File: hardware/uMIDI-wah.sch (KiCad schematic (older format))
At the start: 12 parts, among them U1 Opamp_Dual_Generic

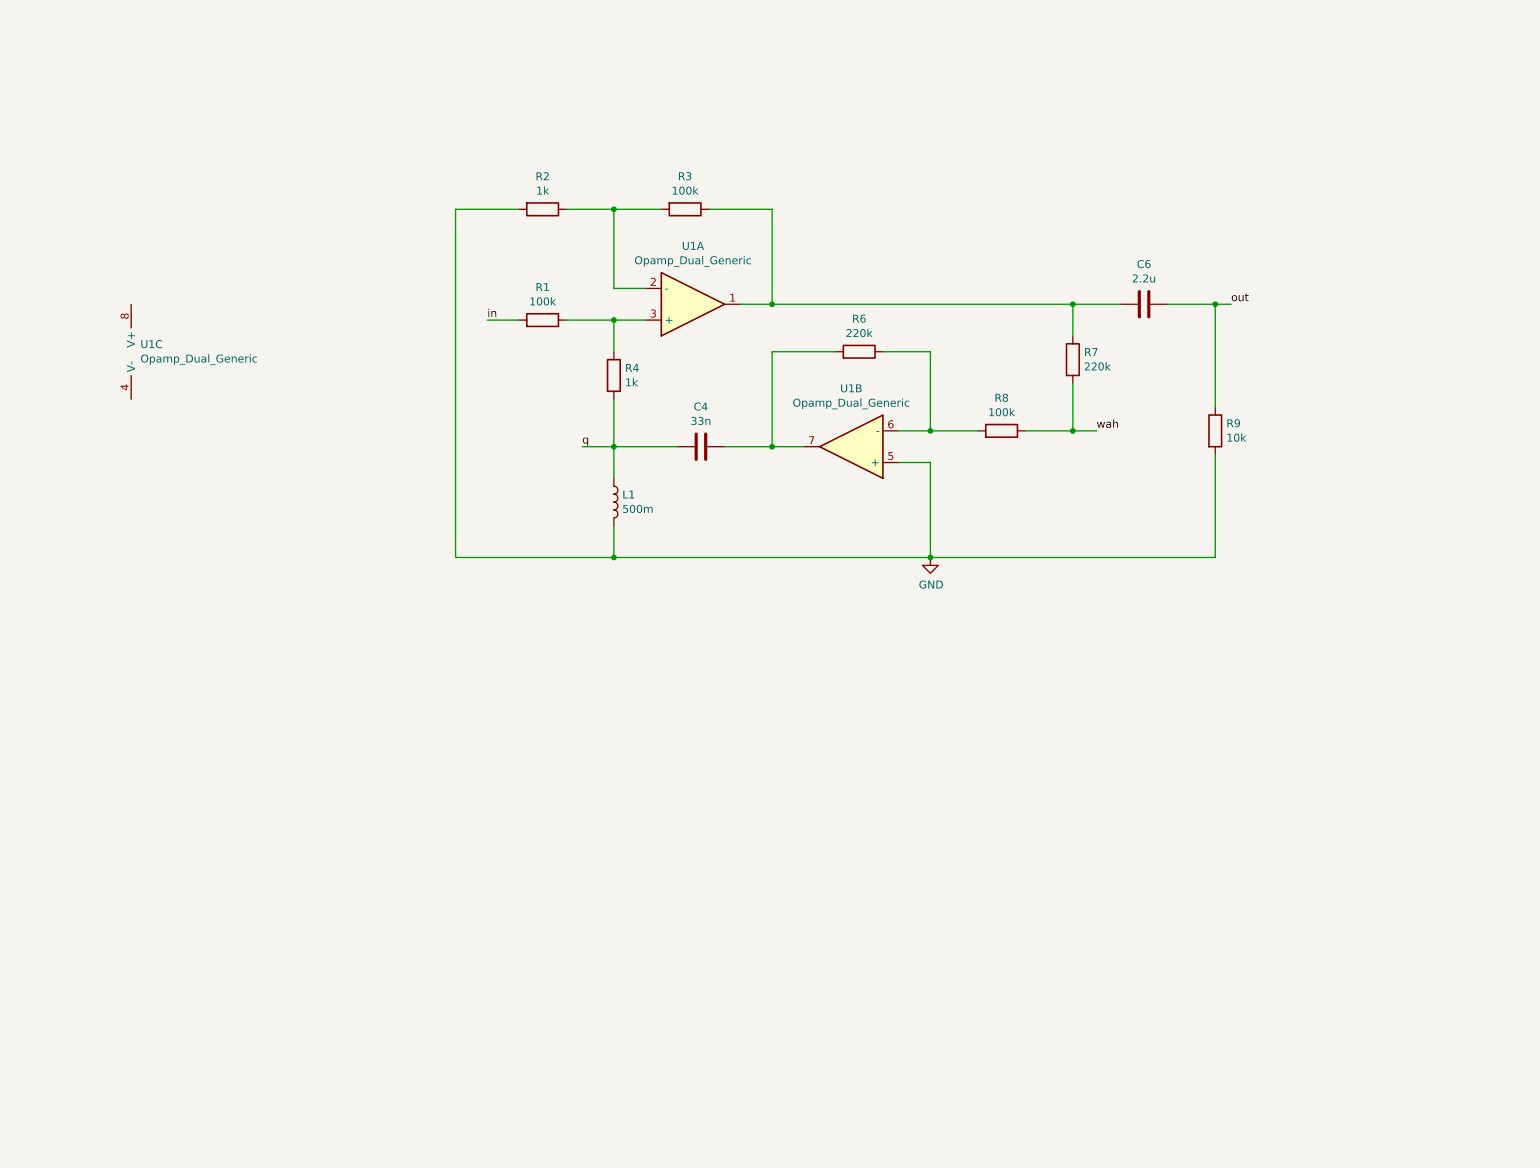
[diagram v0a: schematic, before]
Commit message: Add LED drivers
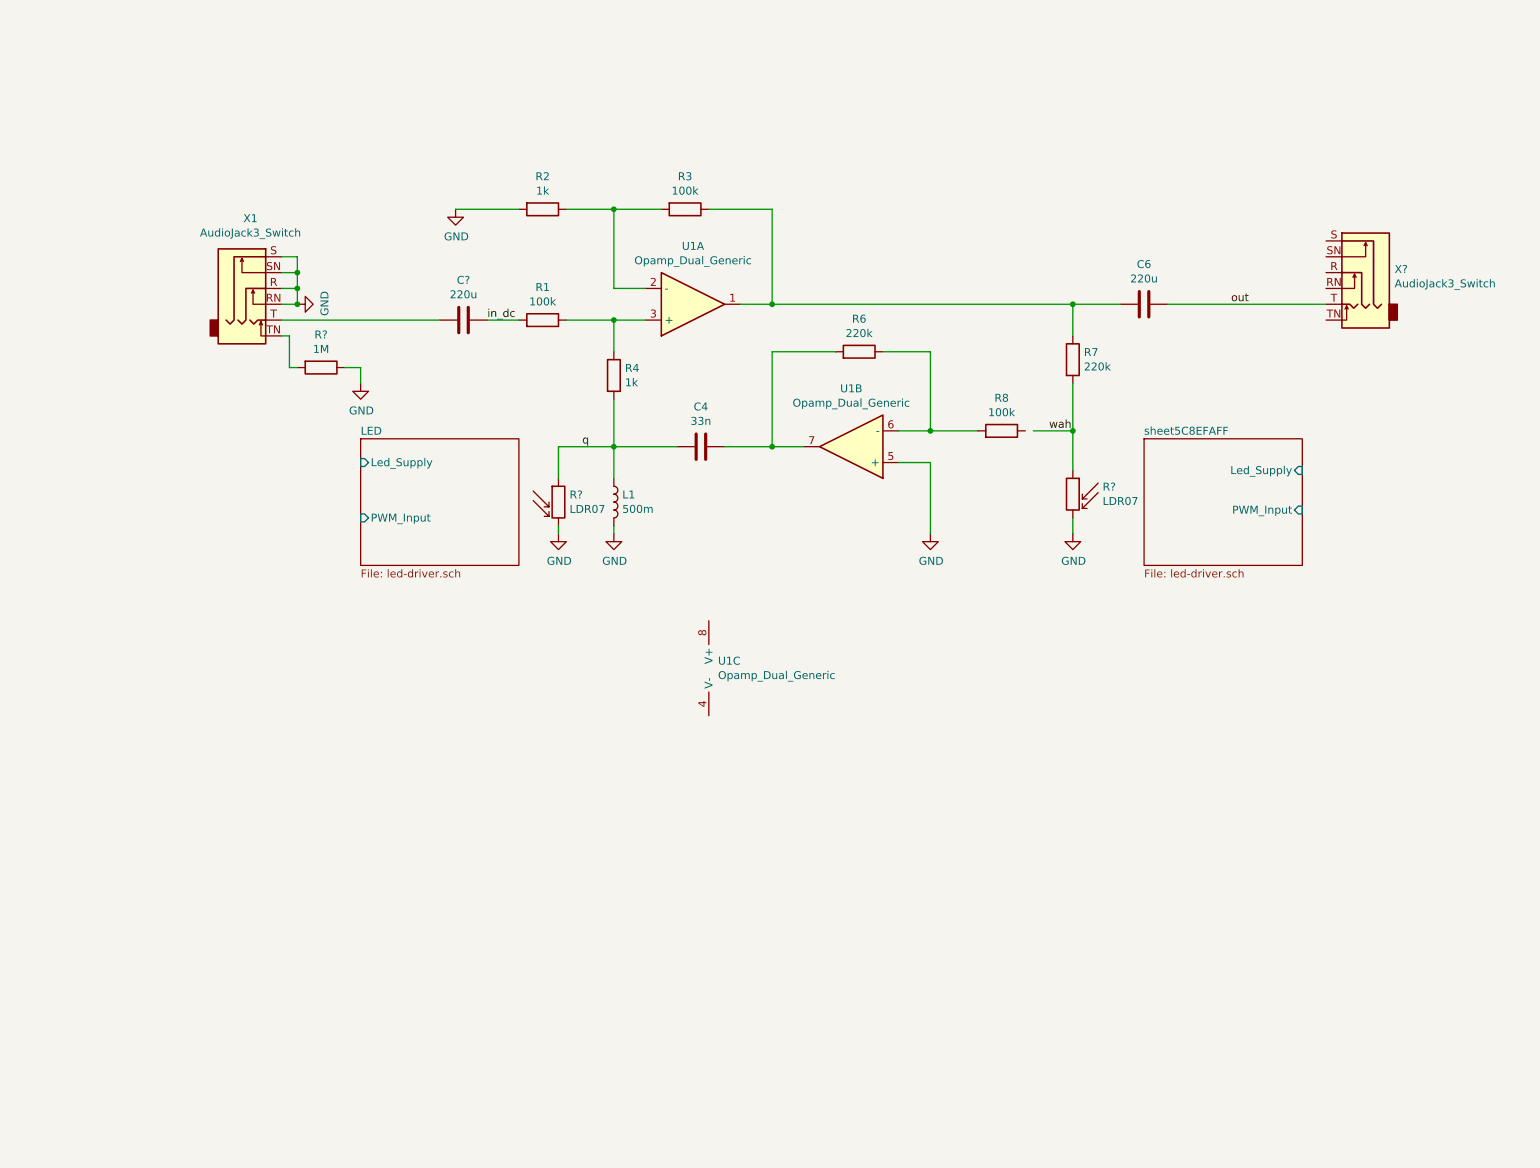
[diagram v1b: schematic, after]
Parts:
- removed R9: 10k, symbol Device:R
- added C?: 220u, symbol Device:C
- added R? (x2): LDR07, OptoDevice:R_LDR_5.1x4.3mm_P3.4mm_Vertical, symbol Sensor_Optical:LDR07
- added R?: 1M, symbol Device:R
- added X1, X?: AudioJack3_Switch, symbol Connector:AudioJack3_Switch
- C6: value 2.2u -> 220u
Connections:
- net GND: now also R?.1, R?.2, R?.2, X1.R, X1.RN, X1.S, X1.SN
- net out: now also X?.T
- net q: now also R?.1
- net wah: now also R?.1; no longer R8.1
- net in renamed in_dc
- net in_dc: now also C?.1
- new net: C?.2, X1.T
- new net: R?.2, X1.TN
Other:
- moved on the sheet: U1C
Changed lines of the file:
@@
 EESchema Schematic File Version 4
+LIBS:uMIDI-wah-cache
 EELAYER 26 0
 EELAYER END
 $Descr A4 11693 8268
 encoding utf-8
-Sheet 1 1
+Sheet 1 2
 Title ""
 Date ""
@@
 $EndComp
 $Comp
-L Device:R R9
-U 1 1 5C8816E9
-P 8600 3100
-F 0 "R9" H 8670 3146 50  0000 L CNN
-F 1 "10k" H 8670 3055 50  0000 L CNN
-F 2 "" V 8530 3100 50  0001 C CNN
-F 3 "~" H 8600 3100 50  0001 C CNN
-	1    8600 3100
-	1    0    0    -1
-$EndComp
-$Comp
 L Device:R R3
 U 1 1 5C88172B
@@
 P 8150 2300
 F 0 "C6" V 7898 2300 50  0000 C CNN
-F 1 "2.2u" V 7989 2300 50  0000 C CNN
+F 1 "220u" V 7989 2300 50  0000 C CNN
 F 2 "" H 8188 2150 50  0001 C CNN
 F 3 "~" H 8150 2300 50  0001 C CNN
@@
 L Device:Opamp_Dual_Generic U1
 U 3 1 5C8825E4
-P 1850 2600
-F 0 "U1" H 1808 2646 50  0000 L CNN
-F 1 "Opamp_Dual_Generic" H 1808 2555 50  0000 L CNN
-F 2 "" H 1850 2600 50  0001 C CNN
-F 3 "~" H 1850 2600 50  0001 C CNN
-	3    1850 2600
+P 5500 4600
+F 0 "U1" H 5458 4646 50  0000 L CNN
+F 1 "Opamp_Dual_Generic" H 5458 4555 50  0000 L CNN
+F 2 "" H 5500 4600 50  0001 C CNN
+F 3 "~" H 5500 4600 50  0001 C CNN
+	3    5500 4600
 	1    0    0    -1
 $EndComp
@@
 Connection ~ 4800 3200
 Wire Wire Line
-	4800 3200 4600 3200
-Wire Wire Line
-	7400 3100 7700 3100
+	7450 3100 7700 3100
 Wire Wire Line
 	6800 3100 7100 3100
@@
 Connection ~ 7700 2300
 Wire Wire Line
-	8700 2300 8600 2300
-Wire Wire Line
-	8600 3900 8600 3250
-Wire Wire Line
 	6600 3300 6800 3300
 Wire Wire Line
-	6800 3300 6800 3900
-Wire Wire Line
-	4800 3700 4800 3900
-Wire Wire Line
-	4800 3900 6800 3900
-Connection ~ 6800 3900
-Connection ~ 4800 3900
+	6800 3300 6800 3750
 $Comp
 L power:GND #PWR?
 U 1 1 5C88B808
-P 6800 3900
-F 0 "#PWR?" H 6800 3650 50  0001 C CNN
-F 1 "GND" H 6805 3727 50  0000 C CNN
-F 2 "" H 6800 3900 50  0001 C CNN
-F 3 "" H 6800 3900 50  0001 C CNN
-	1    6800 3900
-	1    0    0    -1
-$EndComp
-Wire Wire Line
-	3800 1700 3800 3900
+P 6800 3750
+F 0 "#PWR?" H 6800 3500 50  0001 C CNN
+F 1 "GND" H 6805 3577 50  0000 C CNN
+F 2 "" H 6800 3750 50  0001 C CNN
+F 3 "" H 6800 3750 50  0001 C CNN
+	1    6800 3750
+	1    0    0    -1
+$EndComp
 Wire Wire Line
 	3800 1700 4200 1700
@@
 out
 Text Label 4000 2400 0    50   ~ 0
-in
+in_dc
 Wire Wire Line
 	4000 2400 4200 2400
-Wire Wire Line
-	3800 3900 4800 3900
 Text Label 4600 3200 0    50   ~ 0
 q
-Wire Wire Line
-	6800 3900 8600 3900
-Text Label 7850 3100 0    50   ~ 0
+Text Label 7550 3100 0    50   ~ 0
 wah
-Wire Wire Line
-	7850 3100 7700 3100
+$Comp
+L Connector:AudioJack3_Switch X1
+U 1 1 5C8C2F92
+P 2500 2200
+F 0 "X1" H 2504 2642 50  0000 C CNN
+F 1 "AudioJack3_Switch" H 2504 2551 50  0000 C CNN
+F 2 "" H 2500 2200 50  0001 C CNN
+F 3 "~" H 2500 2200 50  0001 C CNN
+	1    2500 2200
+	1    0    0    -1
+$EndComp
+$Comp
+L Sensor_Optical:LDR07 R?
+U 1 1 5C8C34D2
+P 4450 3550
+F 0 "R?" H 4520 3596 50  0000 L CNN
+F 1 "LDR07" H 4520 3505 50  0000 L CNN
+F 2 "OptoDevice:R_LDR_5.1x4.3mm_P3.4mm_Vertical" V 4625 3550 50  0001 C CNN
+F 3 "http://www.tme.eu/de/Document/f2e3ad76a925811312d226c31da4cd7e/LDR07.pdf" H 4450 3500 50  0001 C CNN
+	1    4450 3550
+	1    0    0    -1
+$EndComp
+$Comp
+L Sensor_Optical:LDR07 R?
+U 1 1 5C8C3558
+P 7700 3500
+F 0 "R?" H 7512 3546 50  0000 R CNN
+F 1 "LDR07" H 7512 3455 50  0000 R CNN
+F 2 "OptoDevice:R_LDR_5.1x4.3mm_P3.4mm_Vertical" V 7875 3500 50  0001 C CNN
+F 3 "http://www.tme.eu/de/Document/f2e3ad76a925811312d226c31da4cd7e/LDR07.pdf" H 7700 3450 50  0001 C CNN
+	1    7700 3500
+	-1   0    0    -1
+$EndComp
+Wire Wire Line
+	4450 3400 4450 3200
+Wire Wire Line
+	4450 3200 4800 3200
+$Comp
+L power:GND #PWR?
+U 1 1 5C8C493C
+P 3800 1700
+F 0 "#PWR?" H 3800 1450 50  0001 C CNN
+F 1 "GND" H 3805 1527 50  0000 C CNN
+F 2 "" H 3800 1700 50  0001 C CNN
+F 3 "" H 3800 1700 50  0001 C CNN
+	1    3800 1700
+	1    0    0    -1
+$EndComp
+Wire Wire Line
+	7700 3350 7700 3100
 Connection ~ 7700 3100
-Wire Wire Line
-	8600 2950 8600 2300
-Connection ~ 8600 2300
-Wire Wire Line
-	8600 2300 8300 2300
+$Comp
+L power:GND #PWR?
+U 1 1 5C8C63F2
+P 7700 3750
+F 0 "#PWR?" H 7700 3500 50  0001 C CNN
+F 1 "GND" H 7705 3577 50  0000 C CNN
+F 2 "" H 7700 3750 50  0001 C CNN
+F 3 "" H 7700 3750 50  0001 C CNN
+	1    7700 3750
+	1    0    0    -1
+$EndComp
+Wire Wire Line
+	7700 3750 7700 3650
+$Comp
+L power:GND #PWR?
+U 1 1 5C8C6D5F
+P 4450 3750
+F 0 "#PWR?" H 4450 3500 50  0001 C CNN
+F 1 "GND" H 4455 3577 50  0000 C CNN
+F 2 "" H 4450 3750 50  0001 C CNN
+F 3 "" H 4450 3750 50  0001 C CNN
+	1    4450 3750
+	1    0    0    -1
+$EndComp
+$Comp
+L power:GND #PWR?
+U 1 1 5C8C6D8C
+P 4800 3750
+F 0 "#PWR?" H 4800 3500 50  0001 C CNN
+F 1 "GND" H 4805 3577 50  0000 C CNN
+F 2 "" H 4800 3750 50  0001 C CNN
+F 3 "" H 4800 3750 50  0001 C CNN
+	1    4800 3750
+	1    0    0    -1
+$EndComp
+Wire Wire Line
+	4450 3750 4450 3700
+Wire Wire Line
+	4800 3750 4800 3700
+$Comp
+L Device:C C?
+U 1 1 5C8C9B22
+P 3850 2400
+F 0 "C?" V 3598 2400 50  0000 C CNN
+F 1 "220u" V 3689 2400 50  0000 C CNN
+F 2 "" H 3888 2250 50  0001 C CNN
+F 3 "~" H 3850 2400 50  0001 C CNN
+	1    3850 2400
+	0    1    1    0
+$EndComp
+$Comp
+L Connector:AudioJack3_Switch X?
+U 1 1 5C8CAC4B
+P 9500 2100
+F 0 "X?" H 9267 2121 50  0000 R CNN
+F 1 "AudioJack3_Switch" H 9267 2030 50  0000 R CNN
+F 2 "" H 9500 2100 50  0001 C CNN
+F 3 "~" H 9500 2100 50  0001 C CNN
+	1    9500 2100
+	-1   0    0    -1
+$EndComp
+Wire Wire Line
+	8300 2300 9300 2300
+$Comp
+L Device:R R?
+U 1 1 5C8CF6D3
+P 2950 2700
+F 0 "R?" V 2743 2700 50  0000 C CNN
+F 1 "1M" V 2834 2700 50  0000 C CNN
+F 2 "" V 2880 2700 50  0001 C CNN
+F 3 "~" H 2950 2700 50  0001 C CNN
+	1    2950 2700
+	0    1    1    0
+$EndComp
+Wire Wire Line
+	2700 2300 2800 2300
+Wire Wire Line
+	2800 2300 2800 2200
+Connection ~ 2800 2200
+Wire Wire Line
+	2700 2200 2800 2200
+Wire Wire Line
+	2800 2200 2800 2100
+Wire Wire Line
+	2800 2100 2800 2000
+Connection ~ 2800 2100
+Wire Wire Line
+	2700 2100 2800 2100
+Wire Wire Line
+	2800 2000 2700 2000
+Wire Wire Line
+	3200 2800 3200 2700
+$Comp
+L power:GND #PWR?
+U 1 1 5C8CC597
+P 3200 2800
+F 0 "#PWR?" H 3200 2550 50  0001 C CNN
+F 1 "GND" H 3205 2627 50  0000 C CNN
+F 2 "" H 3200 2800 50  0001 C CNN
+F 3 "" H 3200 2800 50  0001 C CNN
+	1    3200 2800
+	1    0    0    -1
+$EndComp
+Wire Wire Line
+	3700 2400 2700 2400
+Wire Wire Line
+	3100 2700 3200 2700
+$Comp
+L power:GND #PWR?
+U 1 1 5C8D511F
+P 2800 2300
+F 0 "#PWR?" H 2800 2050 50  0001 C CNN
+F 1 "GND" H 2805 2127 50  0000 C CNN
+F 2 "" H 2800 2300 50  0001 C CNN
+F 3 "" H 2800 2300 50  0001 C CNN
+	1    2800 2300
+	0    -1   -1   0
+$EndComp
+Connection ~ 2800 2300
+Wire Wire Line
+	2700 2500 2750 2500
+Wire Wire Line
+	2750 2500 2750 2700
+Wire Wire Line
+	2750 2700 2800 2700
+$Sheet
+S 3200 3150 1000 800
+U 5C8EC687
+F0 "LED" 50
+F1 "led-driver.sch" 50
+F2 "Led_Supply" I L 3200 3300 50
+F3 "PWM_Input" I L 3200 3650 50
+$EndSheet
+$Sheet
+S 8150 3150 1000 800
+U 5C8EFAFF
+F0 "sheet5C8EFAFF" 50
+F1 "led-driver.sch" 50
+F2 "Led_Supply" I R 9150 3350 50
+F3 "PWM_Input" I R 9150 3600 50
+$EndSheet
 $EndSCHEMATC

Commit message: Edit eval schematic; Import bypass
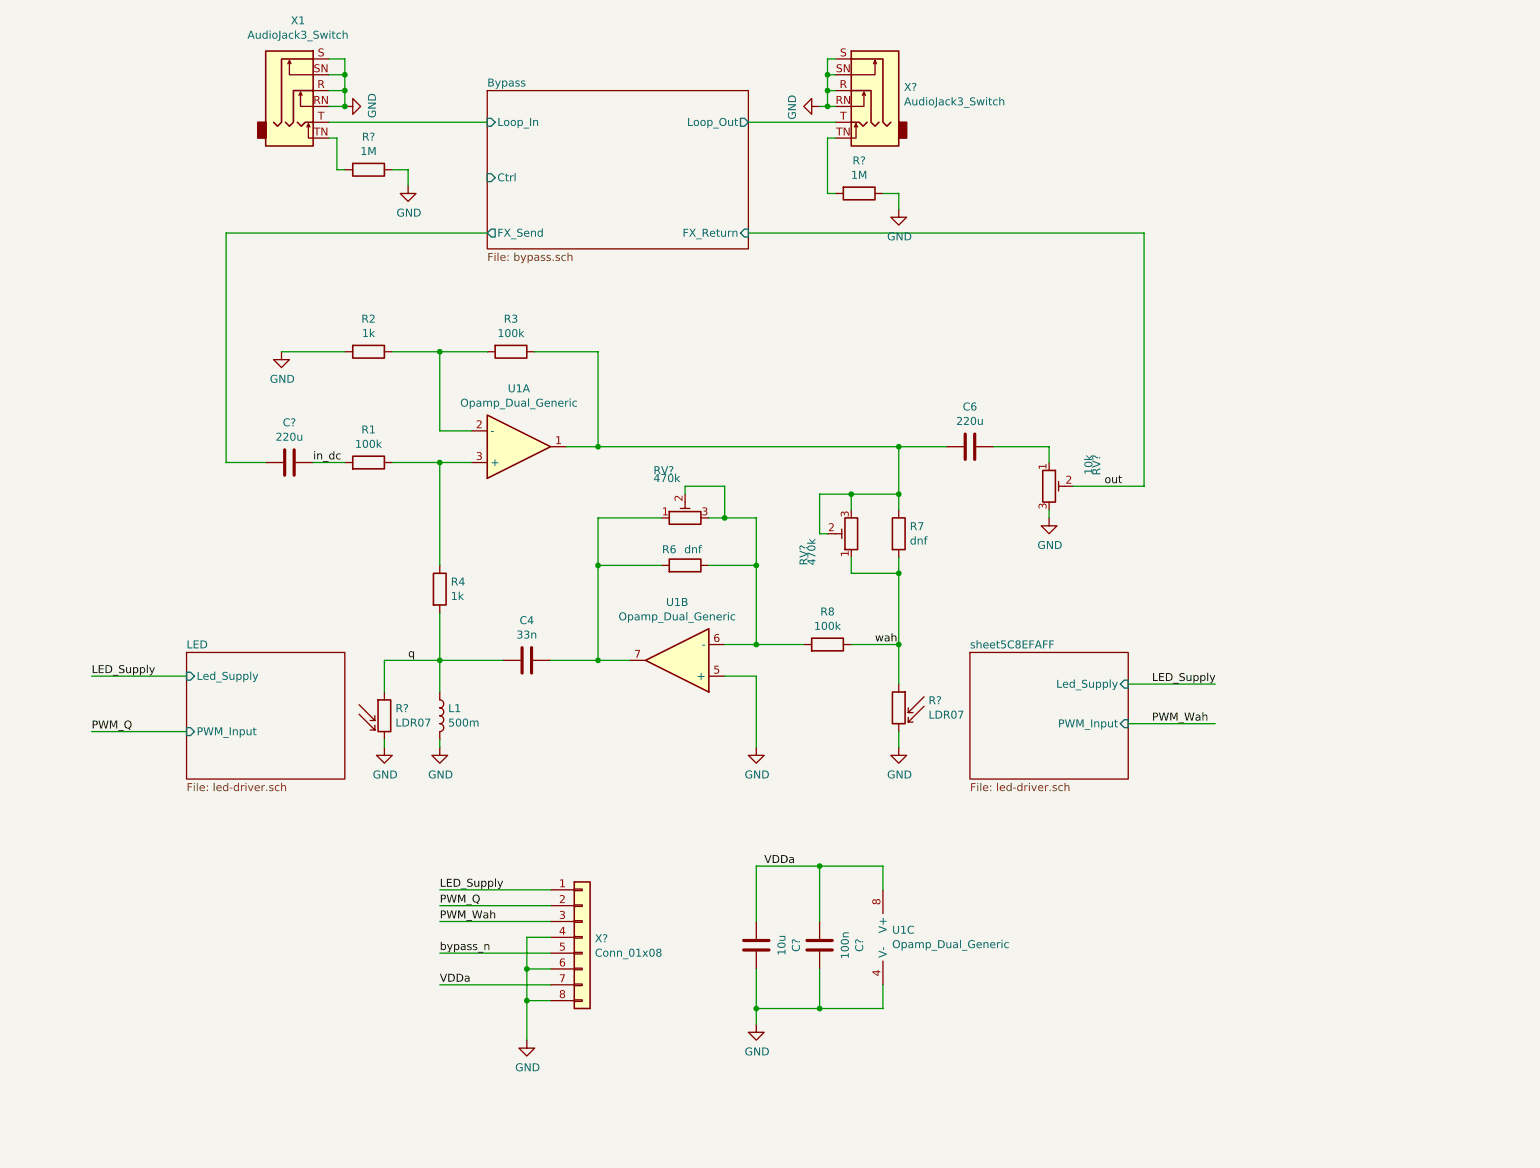
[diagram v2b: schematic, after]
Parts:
- added C?: 100n, symbol Device:C
- added C?: 10u, symbol Device:C
- added R?: 1M, symbol Device:R
- added RV? (x2): 470k, symbol Device:R_POT_TRIM
- added RV?: 10k, symbol Device:R_POT_TRIM
- added X?: Conn_01x08, symbol Connector_Generic:Conn_01x08
- R6, R7: value 220k -> dnf
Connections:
- net GND: now also U1.4 (V-), X?.R, X?.RN, X?.S, X?.SN, C?.1, C?.1, R?.1, RV?.3, X?.4 (Pin_4), X?.6 (Pin_6), X?.8 (Pin_8)
- net out: now also RV?.2; no longer C6.1, X?.T
- net wah: now also R8.1, RV?.1
- net at R6.1, R8.2, U1.6 (-): now also RV?.2, RV?.3
- net at C6.2, R3.1, R7.1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: now also RV?.2, RV?.3
- net at C4.1, R6.2, U1.7: now also RV?.1
- net VDDa: now reaches U1.8 (V+)
- net VDDa: now also C?.2, C?.2, X?.7 (Pin_7)
- net Bypass/FX_Send: now reaches C?.2
- net Bypass/FX_Send: no longer X1.T
- net at X?.TN: now also R?.2
- new net: C6.1, RV?.1
- new net Bypass/Loop_In: X1.T
- new net Bypass/Loop_Out: X?.T
- new net LED_Supply: X?.1 (Pin_1)
- new net PWM_Q: X?.2 (Pin_2)
- new net PWM_Wah: X?.3 (Pin_3)
- new net bypass_n: X?.5 (Pin_5)
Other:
- moved on the sheet: C4, C6, C?, L1, R1, R2, R3, R4, R6, R7, R8, R?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
